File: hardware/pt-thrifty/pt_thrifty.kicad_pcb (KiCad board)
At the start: 2 copper layers, 165.2 x 35.6 mm, 84 parts, among them J1 Conn_01x09, J2 Conn_01x09, J3 SJ-43514-SMT-TR, J4 Conn_01x08, J5 Conn_01x04, J6 Conn_01x02, J81 Conn_01x02, J99 Conn_01x10, SW1 SW_Push_Shielded, SW2 SW_Push_Shielded, SW3 SW_Push_Shielded, U2 MCP6273T, U3 MCP6273T, U4 HT16K33A-28SSOP, U5 HT16K33A-28SSOP, U80 MCP73832-2-OT

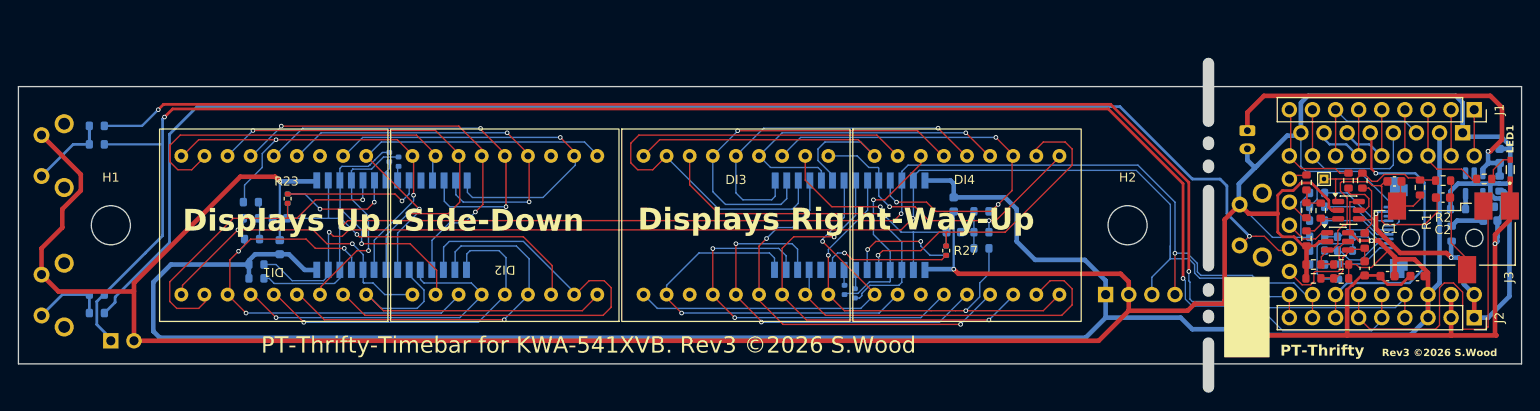
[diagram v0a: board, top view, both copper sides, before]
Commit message: Clean up the Kicad files for PT-Thrifty
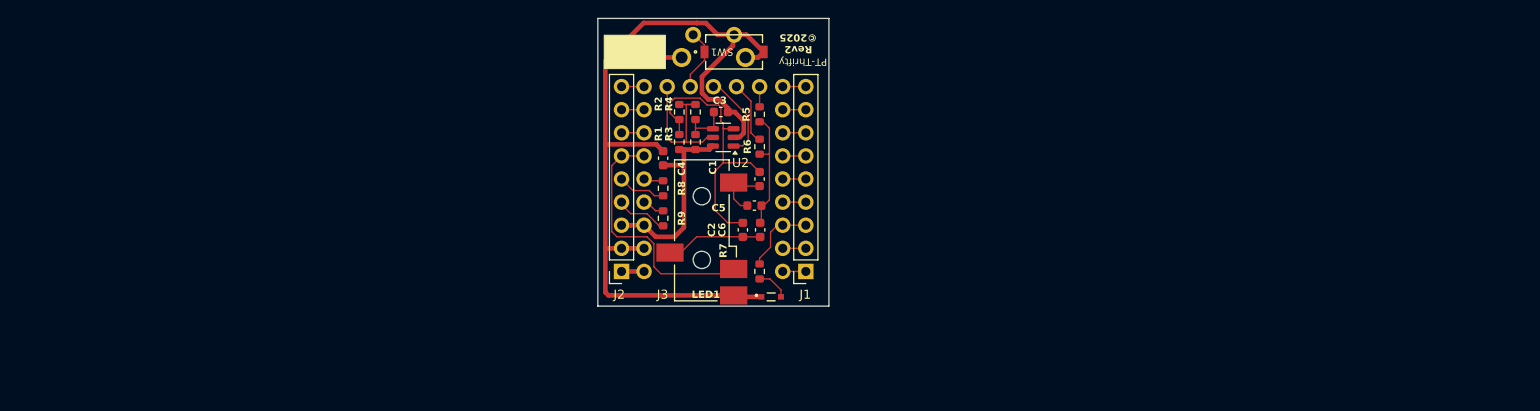
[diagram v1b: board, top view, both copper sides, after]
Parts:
- removed C7, C8: 10uF, Capacitor_SMD:C_0603_1608Metric
- removed C81, C82: 1uF, Capacitor_SMD:C_0603_1608Metric
- removed D1, D2: D, Diode_SMD:D_0603_1608Metric
- removed DI1, DI2, DI3, DI4: KWA-541XVB, Displays:KWA-541XVB
- removed H1, H2: MountingHole, MountingHole:MountingHole_4.3mm_M4
- removed J4: Conn_01x08, Connector_PinSocket_2.54mm:PinSocket_1x08_P2.54mm_Vertical
- removed J5: Conn_01x04, Connector_PinSocket_2.54mm:PinSocket_1x04_P2.54mm_Vertical
- removed J6: Conn_01x02, Connector_PinSocket_2.54mm:PinSocket_1x02_P2.54mm_Vertical
- removed J81: Conn_01x02, Connector_JST:JST_PH_B2B-PH-K_1x02_P2.00mm_Vertical
- removed J99: Conn_01x10, Connector_FFC-FPC:Amphenol_F32Q-1A7x1-11010_1x10-1MP_P0.5mm_Horizontal
- removed R10, R11, R12, R13, R91, R92, R93, R94, R95, R96: 100K, Resistor_SMD:R_0603_1608Metric
- removed R14, R82, R83, R84, R90, R97, R98, R99: 100R, Resistor_SMD:R_0603_1608Metric
- removed R15, R16, R17, R18: 0R, Resistor_SMD:R_0603_1608Metric
- removed R20, R21, R22, R23, R24, R25, R26, R27: 0R, Resistor_SMD:R_0402_1005Metric
- removed R28, R29: 10K, Resistor_SMD:R_0603_1608Metric
- removed R30, R31, R32, R33, R34, R35: 47K, Resistor_SMD:R_0603_1608Metric
- removed R81: 2.00K-1%, Resistor_SMD:R_0603_1608Metric
- removed SW3: SW_Push_Shielded, Button_Switch_THT:SW_Tactile_SPST_Angled_PTS645Vx31-2LFS
- removed TP1: TestPoint, TestPoint:TestPoint_THTPad_1.0x1.0mm_Drill0.5mm
- removed U3: MCP6273T, Package_TO_SOT_SMD:SOT-23-6
- removed U4, U5: HT16K33A-28SSOP, HT9170D:SOIC28-1.27-11.5X17.5MM
- removed U80: MCP73832-2-OT, Package_TO_SOT_SMD:SOT-23-5
- added C6: 100nF, Capacitor_SMD:C_0603_1608Metric, F.Cu at (145.0, 91.9)
- C1, C2, C5: value 1uF -> 100nF
- R1, R2: value 100R -> 10K
- R3, R4: value 100K -> 10K
- R5: value 2.00K-1% -> 2.10K-1%
- R8: value 2.00K-1% -> 22R
- R9: value 2.49K-1% -> 22R
- SW1: value SW_Push_Shielded -> PTS636 SM50J SMTR LFS; footprint Button_Switch_THT:SW_Tactile_SPST_Angled_PTS645Vx31-2LFS -> PicoTimecode_PCB_Rev2:SW_PTS636_CNK; moved to F.Cu
- U2: value MCP6273T -> MCP6273T-E/CH
- moved U1 94.2 mm to (130.9, 98.1), turned to 0 degrees
- moved J2 93.9 mm to (129.8, 96.5), turned to 180 degrees
- moved J3 85.9 mm to (142.1, 99.2), turned to 90 degrees
- moved R2 84.3 mm to (136.1, 79.0), turned to 90 degrees
- moved LED1 82.4 mm to (146.2, 99.3), turned to 0 degrees
- moved R1 81.6 mm to (136.1, 82.3), turned to 90 degrees
- moved C4 80.7 mm to (134.4, 84.1), turned to 90 degrees
- moved SW2 80.6 mm to (142.2, 70.5), turned to 180 degrees
- moved R7 80.3 mm to (145.0, 96.5), turned to -90 degrees
- moved C2 77.0 mm to (143.1, 91.9), turned to 90 degrees
- moved J1 75.6 mm to (150.1, 96.5), turned to 180 degrees
- moved C5 73.3 mm to (144.4, 89.3)
- moved C3 72.8 mm to (140.7, 79.0), turned to 0 degrees
- moved R3 72.2 mm to (137.9, 82.3), turned to 90 degrees
- moved R8 70.7 mm to (134.4, 87.4)
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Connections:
- net /AMP_nEN1 renamed Net-(J1-Pin_9)
- net /I2C1_SCLK renamed Net-(J2-Pin_8)
- net /I2C1_SDA renamed Net-(J2-Pin_9)
- net /SPI0_CSn renamed Net-(J1-Pin_6)
- net /SPI0_DC renamed Net-(J1-Pin_5)
- net /SPI0_RST renamed Net-(J2-Pin_7)
- net /SPI0_SCK renamed Net-(J1-Pin_7)
- net /SPI0_TX renamed Net-(J1-Pin_8)
- C5 pad 1: GND -> /IN_OUT_L
- C5 pad 2: +3.3V -> Net-(C5-Pad2)
- J2 pad 4: /ROT_SW -> Net-(J2-Pin_4)
- J2 pad 5: /CLAP_SW -> Net-(J2-Pin_5)
- R1 pad 1: /OUTPUT -> +3.3V
- R1 pad 2: /IN_OUT_L -> /IN
- R2 pad 1: /OUTPUT -> /IN
- R2 pad 2: /IN_OUT_R -> /AMP_CS
- R3 pad 2: /IN -> /VREF
- R4 pad 1: /IN -> /VREF
- R4 pad 2: GND -> /AMP_CS
- R5 pad 1: +3.3V -> /LTC_TX
- R5 pad 2: /VREF -> Net-(C5-Pad2)
- R6 pad 1: /VREF -> /nLTC_TX
- R6 pad 2: GND -> Net-(C5-Pad2)
- R8 pad 1: /LTC_TX -> Net-(U1-GPIO28)
- R8 pad 2: Net-(R10-Pad1) -> Net-(J2-Pin_5)
- R9 pad 1: /nLTC_TX -> Net-(U1-GPIO29)
- R9 pad 2: Net-(R10-Pad1) -> Net-(J2-Pin_4)
- SW1 pad 1: GND -> /KEYA
- SW1 pad 2: /KEYA -> GND
- SW2 pad 2: Net-(R15-Pad2) -> /KEYA
- U1 pad 14: /CLAP_SW -> Net-(U1-GPIO28)
- U1 pad 15: /ROT_SW -> Net-(U1-GPIO29)
- U1 pad 23: /AMP_nEN0 -> /AMP_CS
- U2 pad 5: /AMP_nEN0 -> /AMP_CS
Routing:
- net GND: track 434.7 -> 101.3 mm, vias 3 -> 0
- net +3.3V: track 264.9 -> 23.4 mm, vias 1 -> 0
- net /CLAP_SW: track 189.8 -> 0.00 mm, vias 2 -> 0
- net /ROT_SW: track 164.4 -> 0.00 mm, vias 2 -> 0
- net /KEYA: track 157.1 -> 6.86 mm, vias 1 -> 0
- net Net-(J2-Pin_8): track 144.0 -> 2.48 mm, vias 3 -> 0
- net Net-(J2-Pin_9): track 143.0 -> 2.48 mm, vias 2 -> 0
- net /time-bar/HM_ROW8: track 57.4 -> 0.00 mm
- net /time-bar/SF_ROW8: track 57.4 -> 0.00 mm
- net /time-bar/HM_ROW2: track 49.5 -> 0.00 mm, vias 2 -> 0
- net /time-bar/HM_ROW0: track 49.3 -> 0.00 mm, vias 3 -> 0
- net /time-bar/SF_ROW2: track 49.1 -> 0.00 mm, vias 2 -> 0
- net /time-bar/SF_ROW0: track 49.1 -> 0.00 mm, vias 3 -> 0
- net /time-bar/SF_ROW3: track 46.4 -> 0.00 mm, vias 2 -> 0
- net /time-bar/HM_ROW3: track 46.4 -> 0.00 mm, vias 2 -> 0
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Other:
- board size 165.2 x 35.6 mm -> 25.4 x 31.6 mm
- board text added: "Rev2 ©2025"
- board text removed: "0"
- board text removed: "0.0"
- board text removed: "0.3"
- board text removed: "0.4"
- board text removed: "0.6"
- board text removed: "0.65"
- board text removed: "0.9"
- board text removed: "1.2 inch"
- board text removed: "16-Segment {dblquote}Time-Bar{dblquote} - for KWA-541XVB modules"
- board text removed: "2026-07-28 © Simon Wood"
- board text removed: "4.8"
- board text removed: "5.2"
- board text removed: "6.5 inch"
- board text removed: "Displays Rig ht-Way-Up"
- board text removed: "Displays Up -Side-Down"
- board text removed: "PT Thrifty - lowest cost TimeCode"
- board text removed: "PT-Thrifty-Timebar for KWA-541XVB. Rev3 ©2026 S.Wood"
- board text removed: "Rev 3"
- board text removed: "Rev3 ©2026 S.Wood"

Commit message: WIP pt-thrifty rev3 sch/pcb
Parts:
- removed C6: 100nF, Capacitor_SMD:C_0603_1608Metric
- added C7: 10uF, Capacitor_SMD:C_0603_1608Metric, B.Cu at (166.3, 89.2)
- added C8: 10uF, Capacitor_SMD:C_0603_1608Metric, B.Cu at (92.2, 93.9)
- added C81: 1uF, Capacitor_SMD:C_0603_1608Metric, B.Cu at (225.3, 90.9)
- added C82: 1uF, Capacitor_SMD:C_0603_1608Metric, B.Cu at (226.3, 83.8)
- added D1: D, Diode_SMD:D_0603_1608Metric, B.Cu at (166.3, 92.2)
- added D2: D, Diode_SMD:D_0603_1608Metric, B.Cu at (92.2, 90.7)
- added DI1: KWA-541XVB, Displays:KWA-541XVB, F.Cu at (91.6, 91.4)
- added DI2: KWA-541XVB, Displays:KWA-541XVB, F.Cu at (117.0, 91.4)
- added DI3: KWA-541XVB, Displays:KWA-541XVB, F.Cu at (142.4, 91.4)
- added DI4: KWA-541XVB, Displays:KWA-541XVB, F.Cu at (167.8, 91.4)
- added H1: MountingHole, MountingHole:MountingHole_4.3mm_M4, F.Cu at (73.7, 91.4)
- added H2: MountingHole, MountingHole:MountingHole_4.3mm_M4, F.Cu at (185.4, 91.4)
- added J4: Conn_01x08, Connector_PinSocket_2.54mm:PinSocket_1x08_P2.54mm_Vertical, B.Cu at (222.2, 81.3)
- added J5: Conn_01x04, Connector_PinSocket_2.54mm:PinSocket_1x04_P2.54mm_Vertical, B.Cu at (183.0, 99.1)
- added J6: Conn_01x02, Connector_PinSocket_2.54mm:PinSocket_1x02_P2.54mm_Vertical, B.Cu at (73.7, 104.1)
- added J81: Conn_01x02, Connector_JST:JST_PH_B2B-PH-K_1x02_P2.00mm_Vertical, B.Cu at (198.6, 81.0)
- added J99: Conn_01x10, Connector_FFC-FPC:Amphenol_F32Q-1A7x1-11010_1x10-1MP_P0.5mm_Horizontal, B.Cu at (217.0, 91.7)
- added R10: 100K, Resistor_SMD:R_0603_1608Metric, F.Cu at (206.7, 89.8)
- added R11: 100K, Resistor_SMD:R_0603_1608Metric, F.Cu at (205.1, 92.9)
- added R12: 100K, Resistor_SMD:R_0603_1608Metric, F.Cu at (211.5, 93.1)
- added R13: 100K, Resistor_SMD:R_0603_1608Metric, F.Cu at (211.2, 86.5)
- added R14: 100R, Resistor_SMD:R_0603_1608Metric, F.Cu at (209.7, 86.5)
- added R15: 0R, Resistor_SMD:R_0603_1608Metric, B.Cu at (72.1, 101.1)
- added R16: 0R, Resistor_SMD:R_0603_1608Metric, B.Cu at (72.1, 99.1)
- added R17: 0R, Resistor_SMD:R_0603_1608Metric, B.Cu at (72.1, 80.5)
- added R18: 0R, Resistor_SMD:R_0603_1608Metric, B.Cu at (72.1, 82.5)
- added R20: 0R, Resistor_SMD:R_0402_1005Metric, B.Cu at (93.1, 88.5)
- added R21: 0R, Resistor_SMD:R_0402_1005Metric, B.Cu at (104.3, 83.9)
- added R22: 0R, Resistor_SMD:R_0402_1005Metric, B.Cu at (105.3, 84.5)
- added R23: 0R, Resistor_SMD:R_0402_1005Metric, F.Cu at (93.1, 88.5)
- added R24: 0R, Resistor_SMD:R_0402_1005Metric, B.Cu at (165.5, 94.2)
- added R25: 0R, Resistor_SMD:R_0402_1005Metric, B.Cu at (155.4, 98.9)
- added R26: 0R, Resistor_SMD:R_0402_1005Metric, B.Cu at (154.3, 98.6)
- added R27: 0R, Resistor_SMD:R_0402_1005Metric, F.Cu at (165.5, 94.2)
- added R28: 10K, Resistor_SMD:R_0603_1608Metric, B.Cu at (89.7, 95.8)
- added R29: 10K, Resistor_SMD:R_0603_1608Metric, B.Cu at (89.7, 97.3)
- added R30: 47K, Resistor_SMD:R_0603_1608Metric, B.Cu at (169.4, 89.9)
- added R31: 47K, Resistor_SMD:R_0603_1608Metric, B.Cu at (169.4, 92.2)
- added R32: 47K, Resistor_SMD:R_0603_1608Metric, B.Cu at (169.4, 94.0)
- added R33: 47K, Resistor_SMD:R_0603_1608Metric, B.Cu at (89.2, 93.0)
- added R34: 47K, Resistor_SMD:R_0603_1608Metric, B.Cu at (89.1, 90.7)
- added R35: 47K, Resistor_SMD:R_0603_1608Metric, B.Cu at (89.1, 88.9)
- added R81: 2.00K-1%, Resistor_SMD:R_0603_1608Metric, B.Cu at (221.7, 89.7)
- added R82: 100R, Resistor_SMD:R_0603_1608Metric, B.Cu at (226.6, 89.4)
- added R83: 100R, Resistor_SMD:R_0603_1608Metric, B.Cu at (221.0, 92.4)
- added R84: 100R, Resistor_SMD:R_0603_1608Metric, B.Cu at (226.3, 86.9)
- added R90: 100R, Resistor_SMD:R_0603_1608Metric, B.Cu at (222.4, 96.4)
- added R91: 100K, Resistor_SMD:R_0603_1608Metric, B.Cu at (208.5, 96.5)
- added R92: 100K, Resistor_SMD:R_0603_1608Metric, B.Cu at (206.3, 95.8)
- added R93: 100K, Resistor_SMD:R_0603_1608Metric, B.Cu at (209.3, 94.2)
- added R94: 100K, Resistor_SMD:R_0603_1608Metric, B.Cu at (206.3, 94.2)
- added R95: 100K, Resistor_SMD:R_0603_1608Metric, B.Cu at (209.3, 92.7)
- added R96: 100K, Resistor_SMD:R_0603_1608Metric, B.Cu at (206.3, 92.7)
- added R97: 100R, Resistor_SMD:R_0603_1608Metric, B.Cu at (206.2, 90.9)
- added R98: 100R, Resistor_SMD:R_0603_1608Metric, B.Cu at (206.2, 89.4)
- added R99: 100R, Resistor_SMD:R_0603_1608Metric, B.Cu at (206.2, 87.9)
- added SW3: SW_Push_Shielded, Button_Switch_THT:SW_Tactile_SPST_Angled_PTS645Vx31-2LFS, B.Cu at (66.0, 81.5)
- added TP1: TestPoint, TestPoint:TestPoint_THTPad_1.0x1.0mm_Drill0.5mm, F.Cu at (207.0, 86.4)
- added U3: MCP6273T, Package_TO_SOT_SMD:SOT-23-6, F.Cu at (209.7, 89.8)
- added U4: HT16K33A-28SSOP, HT9170D:SOIC28-1.27-11.5X17.5MM, B.Cu at (154.9, 91.4)
- added U5: HT16K33A-28SSOP, HT9170D:SOIC28-1.27-11.5X17.5MM, B.Cu at (104.5, 91.4)
- added U80: MCP73832-2-OT, Package_TO_SOT_SMD:SOT-23-5, B.Cu at (223.5, 86.9)
- C1, C2, C5: value 100nF -> 1uF
- R1, R2: value 10K -> 100R
- R3, R4: value 10K -> 100K
- R5: value 2.10K-1% -> 2.00K-1%
- R8: value 22R -> 2.00K-1%
- R9: value 22R -> 2.49K-1%
- SW1: value PTS636 SM50J SMTR LFS -> SW_Push_Shielded; footprint PicoTimecode_PCB_Rev2:SW_PTS636_CNK -> Button_Switch_THT:SW_Tactile_SPST_Angled_PTS645Vx31-2LFS; moved to B.Cu
- U2: value MCP6273T-E/CH -> MCP6273T
- moved U1 94.2 mm to (225.1, 100.4), turned to 90 degrees
- moved J2 93.9 mm to (223.5, 101.6), turned to -90 degrees
- moved J3 85.9 mm to (227.4, 89.3), turned to 180 degrees
- moved R2 84.3 mm to (220.1, 86.5), turned to 0 degrees
- moved LED1 82.4 mm to (227.5, 85.3), turned to 90 degrees
- moved R1 81.6 mm to (217.6, 87.3), turned to -90 degrees
- moved C4 80.7 mm to (214.0, 97.0), turned to 180 degrees
- moved SW2 80.6 mm to (66.0, 96.9), turned to -90 degrees
- moved R7 80.3 mm to (224.6, 86.4), turned to 0 degrees
- moved C2 77.0 mm to (220.1, 88.4), turned to 180 degrees
- moved J1 75.6 mm to (223.5, 78.7), turned to -90 degrees
- moved C5 73.3 mm to (217.3, 97.0)
- moved C3 72.8 mm to (211.5, 96.2), turned to -90 degrees
- moved R3 72.2 mm to (208.9, 95.8), turned to 180 degrees
- moved R8 70.7 mm to (205.1, 86.7)
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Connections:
- net Net-(J1-Pin_5) renamed /SPI0_DC
- net Net-(J1-Pin_6) renamed /SPI0_CSn
- net Net-(J1-Pin_7) renamed /SPI0_SCK
- net Net-(J1-Pin_8) renamed /SPI0_TX
- net Net-(J1-Pin_9) renamed /AMP_nEN1
- net Net-(J2-Pin_7) renamed /SPI0_RST
- net Net-(J2-Pin_8) renamed /I2C1_SCLK
- net Net-(J2-Pin_9) renamed /I2C1_SDA
- C5 pad 1: /IN_OUT_L -> GND
- C5 pad 2: Net-(C5-Pad2) -> +3.3V
- J2 pad 4: Net-(J2-Pin_4) -> /ROT_SW
- J2 pad 5: Net-(J2-Pin_5) -> /CLAP_SW
- R1 pad 1: +3.3V -> /OUTPUT
- R1 pad 2: /IN -> /IN_OUT_L
- R2 pad 1: /IN -> /OUTPUT
- R2 pad 2: /AMP_CS -> /IN_OUT_R
- R3 pad 2: /VREF -> /IN
- R4 pad 1: /VREF -> /IN
- R4 pad 2: /AMP_CS -> GND
- R5 pad 1: /LTC_TX -> +3.3V
- R5 pad 2: Net-(C5-Pad2) -> /VREF
- R6 pad 1: /nLTC_TX -> /VREF
- R6 pad 2: Net-(C5-Pad2) -> GND
- R8 pad 1: Net-(U1-GPIO28) -> /LTC_TX
- R8 pad 2: Net-(J2-Pin_5) -> Net-(R10-Pad1)
- R9 pad 1: Net-(U1-GPIO29) -> /nLTC_TX
- R9 pad 2: Net-(J2-Pin_4) -> Net-(R10-Pad1)
- SW1 pad 1: /KEYA -> GND
- SW1 pad 2: GND -> /KEYA
- SW2 pad 2: /KEYA -> Net-(R15-Pad2)
- U1 pad 14: Net-(U1-GPIO28) -> /CLAP_SW
- U1 pad 15: Net-(U1-GPIO29) -> /ROT_SW
- U1 pad 23: /AMP_CS -> /AMP_nEN0
- U2 pad 5: /AMP_CS -> /AMP_nEN0
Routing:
- net GND: track 101.3 -> 434.7 mm, vias 0 -> 3
- net +3.3V: track 23.4 -> 264.9 mm, vias 0 -> 1
- net /CLAP_SW: track 0.00 -> 189.8 mm, vias 0 -> 2
- net /ROT_SW: track 0.00 -> 164.4 mm, vias 0 -> 2
- net /KEYA: track 6.86 -> 157.1 mm, vias 0 -> 1
- net /I2C1_SCLK: track 2.48 -> 144.0 mm, vias 0 -> 3
- net /I2C1_SDA: track 2.48 -> 143.0 mm, vias 0 -> 2
- net /time-bar/HM_ROW8: track 0.00 -> 57.4 mm
- net /time-bar/SF_ROW8: track 0.00 -> 57.4 mm
- net /time-bar/HM_ROW2: track 0.00 -> 49.5 mm, vias 0 -> 2
- net /time-bar/HM_ROW0: track 0.00 -> 49.3 mm, vias 0 -> 3
- net /time-bar/SF_ROW2: track 0.00 -> 49.1 mm, vias 0 -> 2
- net /time-bar/SF_ROW0: track 0.00 -> 49.1 mm, vias 0 -> 3
- net /time-bar/SF_ROW3: track 0.00 -> 46.4 mm, vias 0 -> 2
- net /time-bar/HM_ROW3: track 0.00 -> 46.4 mm, vias 0 -> 2
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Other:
- board size 25.4 x 31.6 mm -> 165.2 x 35.6 mm
- board text added: "0"
- board text added: "0.0"
- board text added: "0.3"
- board text added: "0.4"
- board text added: "0.6"
- board text added: "0.65"
- board text added: "0.9"
- board text added: "1.2 inch"
- board text added: "16-Segment {dblquote}Time-Bar{dblquote} - for KWA-541XVB modules"
- board text added: "2026-07-28 © Simon Wood"
- board text added: "4.8"
- board text added: "5.2"
- board text added: "6.5 inch"
- board text added: "Displays Rig ht-Way-Up"
- board text added: "Displays Up -Side-Down"
- board text added: "PT Thrifty - lowest cost TimeCode"
- board text added: "PT-Thrifty-Timebar for KWA-541XVB. Rev3 ©2026 S.Wood"
- board text added: "Rev 3"
- board text added: "Rev3 ©2026 S.Wood"
- board text removed: "Rev2 ©2025"
